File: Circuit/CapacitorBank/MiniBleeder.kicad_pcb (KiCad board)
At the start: 2 copper layers, 71.1 x 15.2 mm, 27 parts, among them J1 Signal 1/3, J2 Signal 2/4, J3 Power

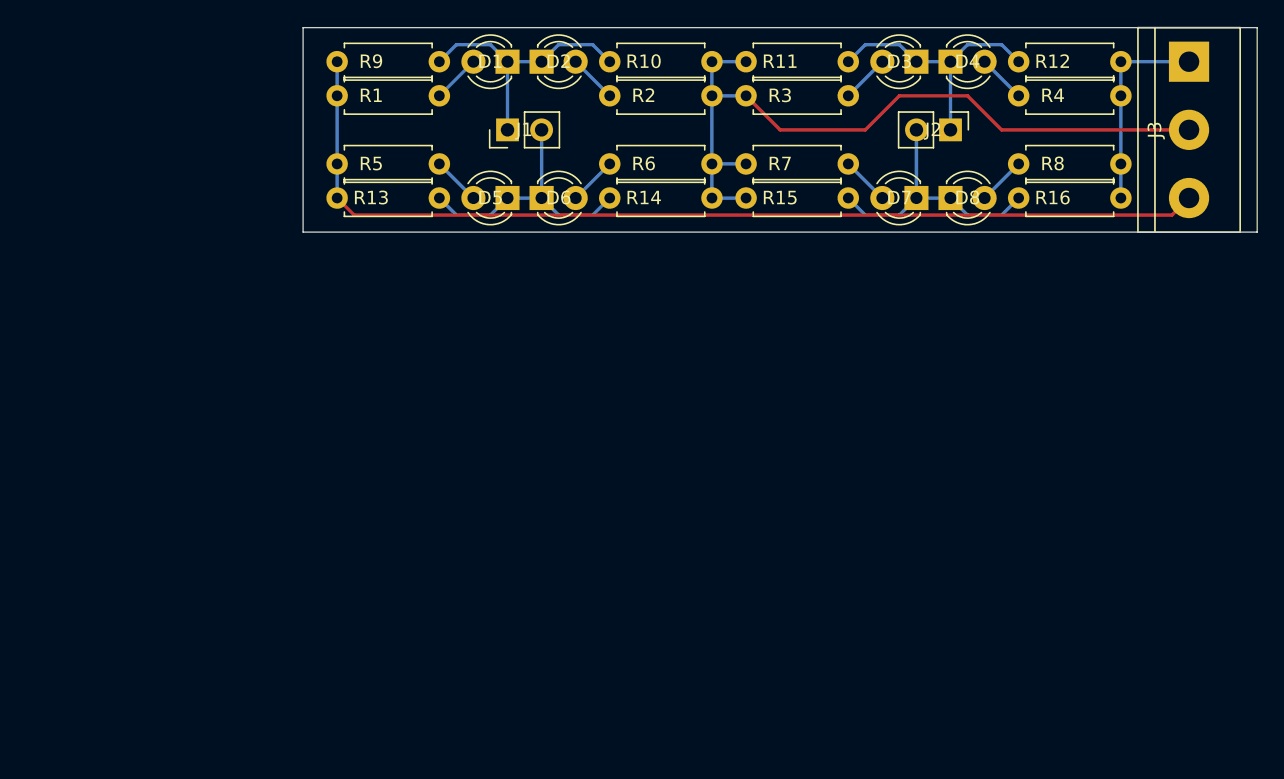
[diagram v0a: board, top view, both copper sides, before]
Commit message: [Circuit] Polarized capacitor bank and bleeder
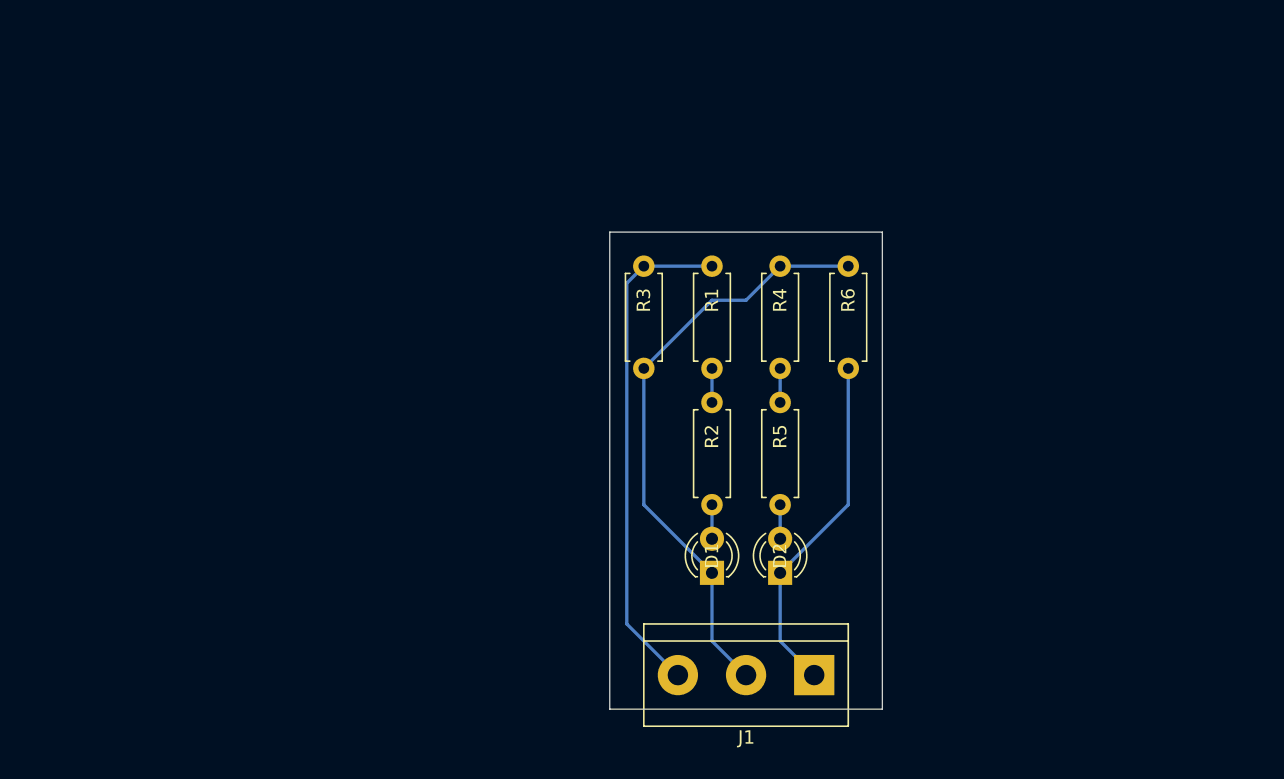
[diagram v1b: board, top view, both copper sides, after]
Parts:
- removed the D2 at (68.6, 53.3)
- removed D4, D5, D6, D7, D8: LED, LED_THT:LED_D3.0mm_FlatTop
- removed J2: Signal 2/4, Connector_PinHeader_2.54mm:PinHeader_1x02_P2.54mm_Vertical
- removed J3: Power, TerminalBlock:TerminalBlock_bornier-3_P5.08mm
- removed R10, R11, R12, R13, R14, R15, R16, R7, R8: 6.8K, Resistor_THT:R_Axial_DIN0207_L6.3mm_D2.5mm_P7.62mm_Horizontal
- removed the R3 at (83.8, 55.9)
- J1: value Signal 1/3 -> From Capacitor Bank; footprint Connector_PinHeader_2.54mm:PinHeader_1x02_P2.54mm_Vertical -> TerminalBlock:TerminalBlock_bornier-3_P5.08mm
- R1, R4: value 6.8K -> 10K
- R2, R5: value 6.8K -> 3.3K
- R3: renamed from R9; value 6.8K -> 20K
- R6: value 6.8K -> 20K
- moved J1 46.6 mm to (88.9, 99.1), turned to 180 degrees
- moved D1 41.0 mm to (81.3, 91.4), turned to 90 degrees
- moved D2 39.4 mm to (86.4, 91.4), turned to 90 degrees
- moved R5 37.5 mm to (86.4, 78.7), turned to 270 degrees
- moved R1 30.7 mm to (81.3, 68.6), turned to 270 degrees
- moved R3 27.5 mm to (76.2, 68.6), turned to 270 degrees
- moved R2 24.1 mm to (81.3, 78.7), turned to 270 degrees
- moved R4 21.8 mm to (86.4, 68.6), turned to 270 degrees
- moved R6 19.3 mm to (91.4, 68.6), turned to 270 degrees
- renumbered D3 to D2
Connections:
- D1 pad 1: Net-(D1-Pad1) -> /CapacitorCenter
- D2 pad 1: Net-(D3-Pad1) -> /CapacitorPower-
- D2 pad 2: Net-(D3-Pad2) -> Net-(D2-Pad2)
- J1 pad 1: Net-(D1-Pad1) -> /CapacitorPower-
- J1 pad 2: Net-(D5-Pad1) -> /CapacitorCenter
- R1 pad 1: +VDC -> /CapacitorPower+
- R1 pad 2: Net-(D1-Pad2) -> Net-(R1-Pad2)
- R2 pad 1: Net-(D2-Pad2) -> Net-(R1-Pad2)
- R2 pad 2: GND -> Net-(D1-Pad2)
- R3 pad 1: +VDC -> /CapacitorPower+
- R3 pad 2: Net-(D1-Pad1) -> /CapacitorCenter
- R4 pad 1: Net-(D4-Pad2) -> /CapacitorCenter
- R4 pad 2: -VDC -> Net-(R4-Pad2)
- R5 pad 1: +VDC -> Net-(R4-Pad2)
- R5 pad 2: Net-(D5-Pad2) -> Net-(D2-Pad2)
- R6 pad 1: Net-(D6-Pad2) -> /CapacitorCenter
- R6 pad 2: GND -> /CapacitorPower-
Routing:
- net +VDC: track 74.7 -> 0.00 mm
- net GND: track 56.5 -> 0.00 mm
- net /CapacitorCenter: track 0.00 -> 44.4 mm
- net /CapacitorPower+: track 0.00 -> 37.7 mm
- net /CapacitorPower-: track 0.00 -> 26.0 mm
- net Net-(D3-Pad1): track 19.9 -> 0.00 mm
- net Net-(D1-Pad1): track 19.9 -> 0.00 mm
- net Net-(D7-Pad1): track 19.9 -> 0.00 mm
- net Net-(D5-Pad1): track 19.9 -> 0.00 mm
- net -VDC: track 15.2 -> 0.00 mm
- net Net-(D8-Pad2): track 3.59 -> 0.00 mm
- net Net-(D7-Pad2): track 3.59 -> 0.00 mm
- net Net-(D4-Pad2): track 3.59 -> 0.00 mm
- net Net-(D3-Pad2): track 3.59 -> 0.00 mm
- net Net-(D5-Pad2): track 3.59 -> 0.00 mm
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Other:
- board size 71.1 x 15.2 mm -> 20.3 x 35.6 mm

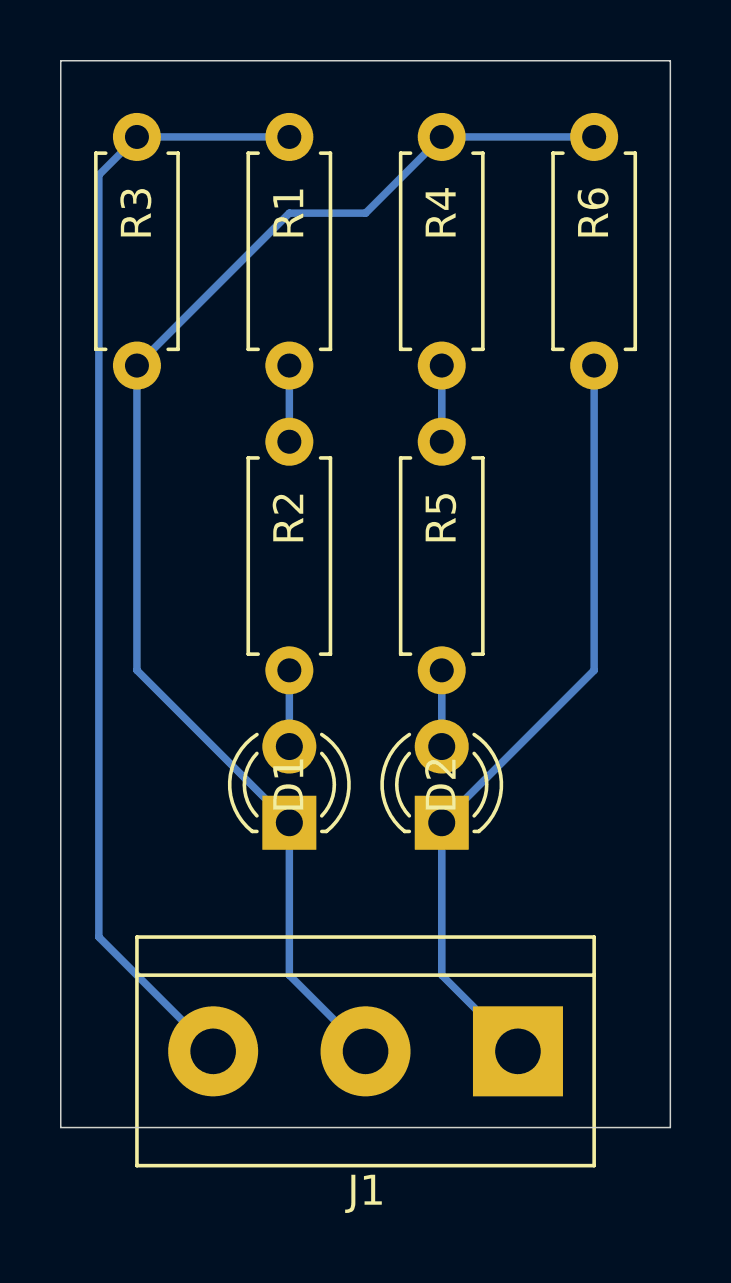
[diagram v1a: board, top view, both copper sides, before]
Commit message: [Circuit] Update the numbers in capacitor bank subsystem
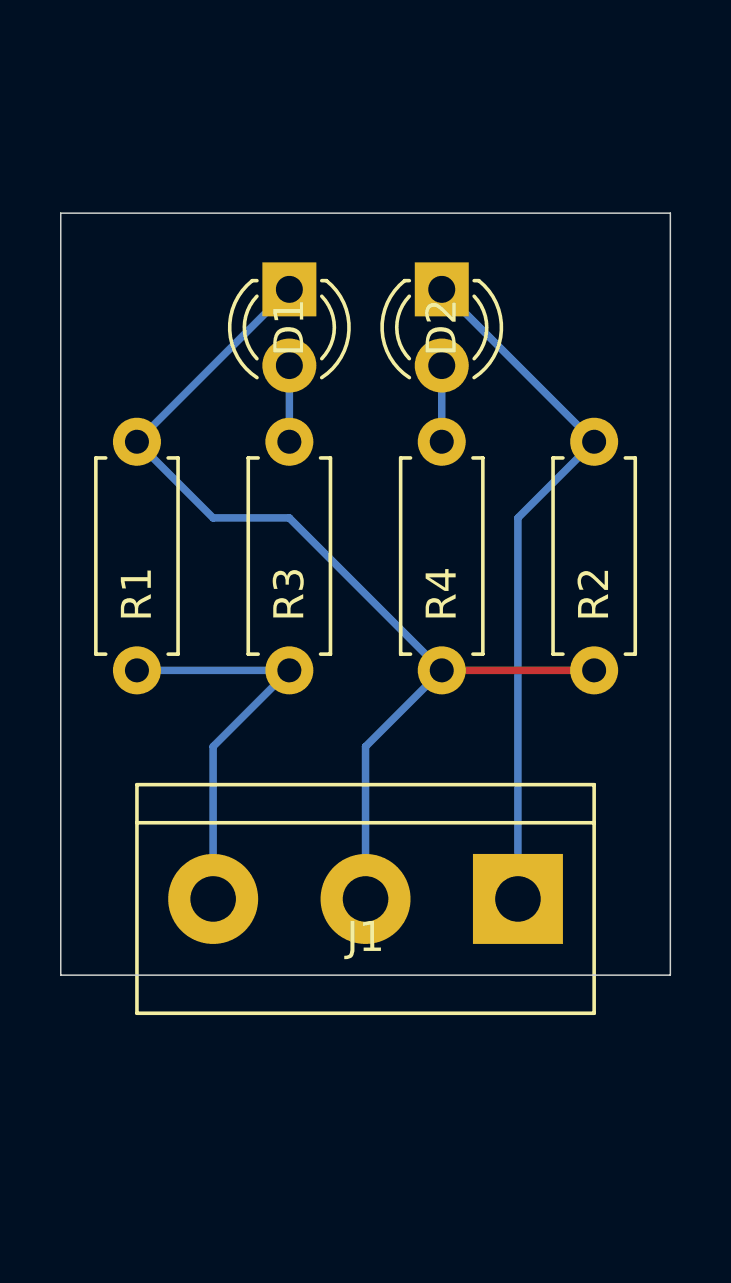
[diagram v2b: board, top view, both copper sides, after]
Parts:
- removed the R3 at (76.2, 68.6)
- removed the R4 at (86.4, 68.6)
- removed R6: 20K, Resistor_THT:R_Axial_DIN0207_L6.3mm_D2.5mm_P7.62mm_Horizontal
- added R2: 20K, Resistor_THT:R_Axial_DIN0207_L6.3mm_D2.5mm_P7.62mm_Horizontal, F.Cu at (91.4, 86.4)
- R1: value 10K -> 20K
- moved R1 18.5 mm to (76.2, 86.4), turned to 90 degrees
- moved D1 17.8 mm to (81.3, 73.7), turned to 270 degrees
- moved D2 17.8 mm to (86.4, 73.7), turned to 270 degrees
- moved R3 7.62 mm to (81.3, 86.4), turned to 90 degrees
- moved R4 7.62 mm to (86.4, 86.4), turned to 90 degrees
- moved J1 5.08 mm to (88.9, 94.0)
- renumbered R2 to R3, R5 to R4
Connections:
- R1 pad 2: Net-(R1-Pad2) -> /CapacitorCenter
- R3 pad 1: Net-(R1-Pad2) -> /CapacitorPower+
- R4 pad 1: Net-(R4-Pad2) -> /CapacitorCenter
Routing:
- net /CapacitorPower+: track 37.7 -> 13.8 mm
- net /CapacitorCenter: track 44.4 -> 34.3 mm
- net /CapacitorPower-: track 26.0 -> 23.5 mm
- net Net-(R4-Pad2): track 2.54 -> 0.00 mm
- net Net-(R1-Pad2): track 2.54 -> 0.00 mm
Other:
- board size 20.3 x 35.6 mm -> 20.3 x 25.4 mm

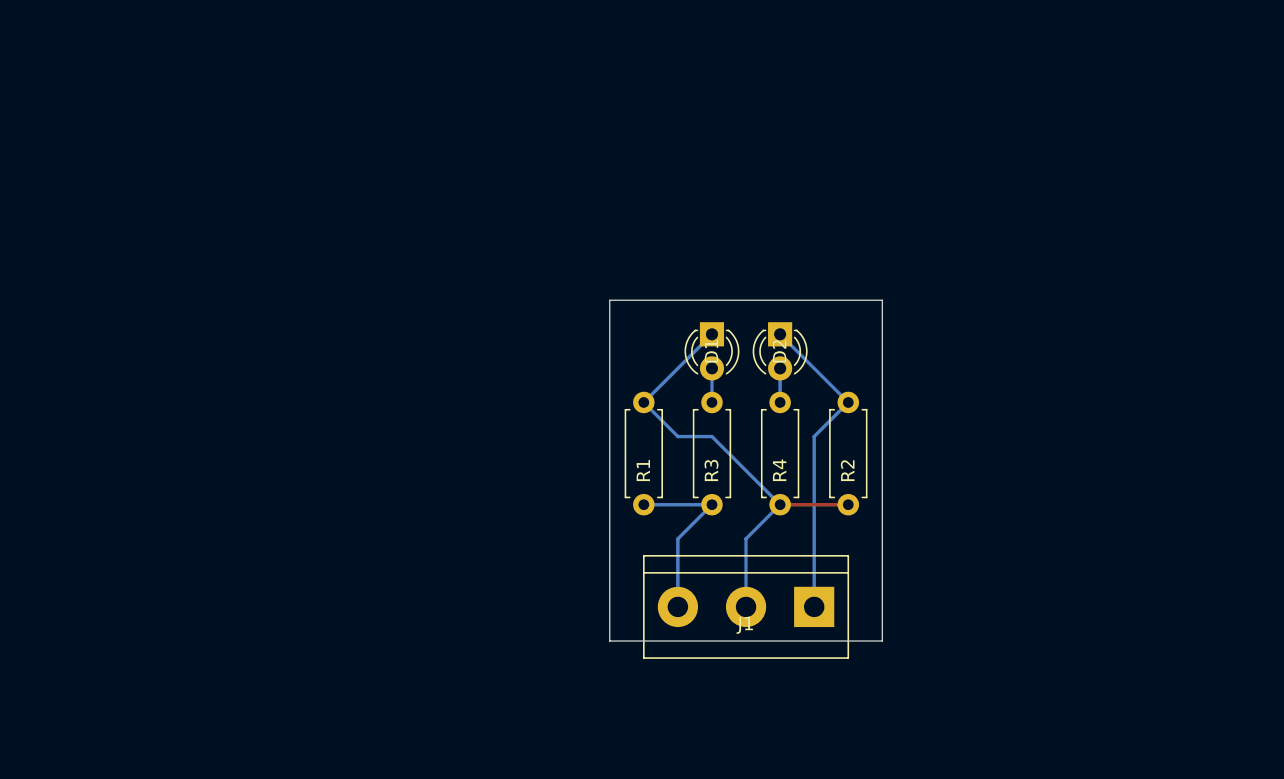
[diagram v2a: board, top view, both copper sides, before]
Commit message: [Circuit] Add isolated switches to bleeder circuits
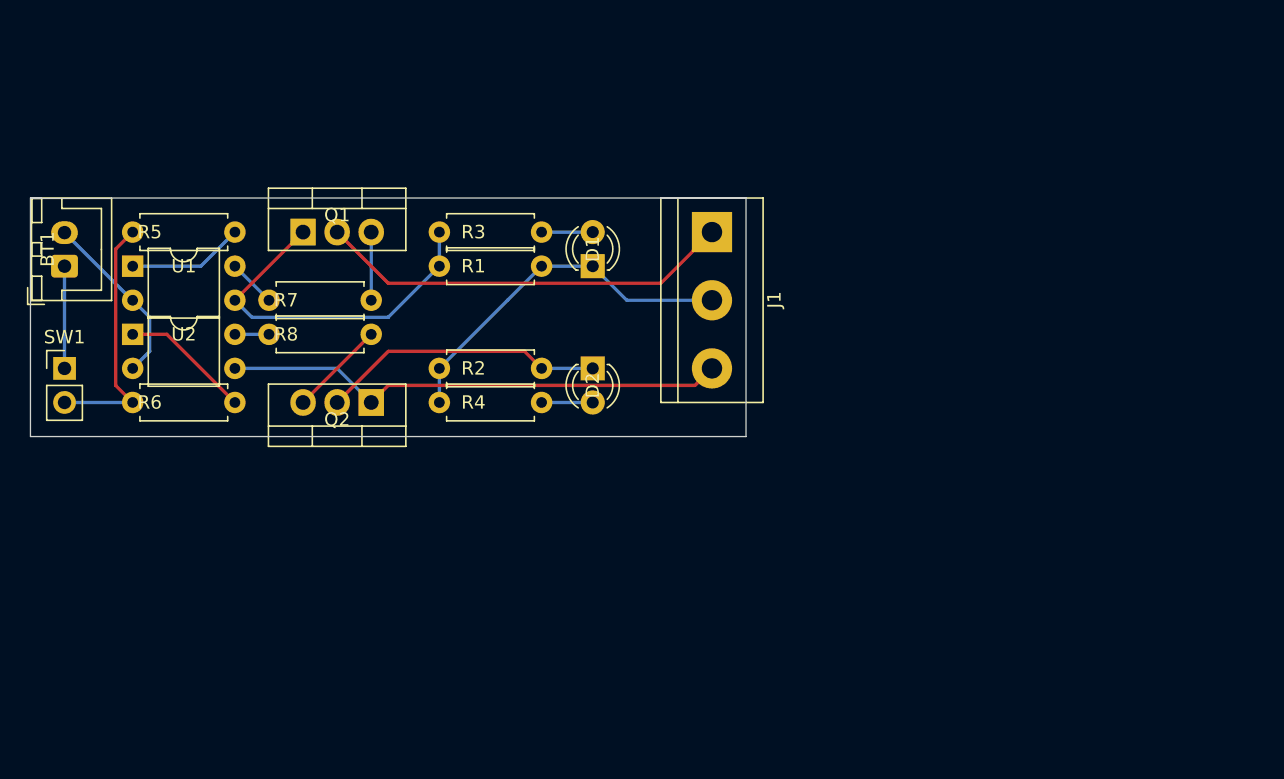
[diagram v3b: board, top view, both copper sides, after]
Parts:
- added BT1: 12V Battery, Connector_JST:JST_XH_B2B-XH-A_1x02_P2.50mm_Vertical, F.Cu at (33.0, 68.6)
- added Q1: BT138-800, Package_TO_SOT_THT:TO-220-3_Vertical, F.Cu at (50.8, 66.0)
- added Q2: BT138-800, Package_TO_SOT_THT:TO-220-3_Vertical, F.Cu at (55.9, 78.7)
- added R5: 1K, Resistor_THT:R_Axial_DIN0207_L6.3mm_D2.5mm_P7.62mm_Horizontal, F.Cu at (38.1, 66.0)
- added R6: 1K, Resistor_THT:R_Axial_DIN0207_L6.3mm_D2.5mm_P7.62mm_Horizontal, F.Cu at (38.1, 78.7)
- added R7: 1K, Resistor_THT:R_Axial_DIN0207_L6.3mm_D2.5mm_P7.62mm_Horizontal, F.Cu at (55.9, 71.1)
- added R8: 1K, Resistor_THT:R_Axial_DIN0207_L6.3mm_D2.5mm_P7.62mm_Horizontal, F.Cu at (55.9, 73.7)
- added SW1: SW_Push, Connector_PinHeader_2.54mm:PinHeader_1x02_P2.54mm_Vertical, F.Cu at (33.0, 76.2)
- added U1: PC817, Package_DIP:DIP-4_W7.62mm, F.Cu at (38.1, 68.6)
- added U2: PC817, Package_DIP:DIP-4_W7.62mm, F.Cu at (38.1, 73.7)
- moved R2 32.1 mm to (61.0, 76.2), turned to 0 degrees
- moved J1 29.0 mm to (81.3, 66.0), turned to 270 degrees
- moved R3 28.7 mm to (61.0, 66.0), turned to 0 degrees
- moved R4 26.5 mm to (61.0, 78.7), turned to 0 degrees
- moved R1 23.4 mm to (61.0, 68.6), turned to 0 degrees
- moved D2 14.2 mm to (72.4, 76.2)
- moved D1 10.2 mm to (72.4, 68.6), turned to 90 degrees
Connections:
- D2 pad 1: /CapacitorPower- -> Net-(D2-Pad1)
- J1 pad 1: /CapacitorPower- -> /CapacitorPower+
- J1 pad 3: /CapacitorPower+ -> /CapacitorPower-
- R1 pad 1: /CapacitorPower+ -> Net-(Q1-Pad1)
- R2 pad 2: /CapacitorPower- -> Net-(D2-Pad1)
- R3 pad 1: /CapacitorPower+ -> Net-(Q1-Pad1)
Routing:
- net Net-(Q1-Pad1): track 0.00 -> 27.1 mm
- net Net-(D2-Pad1): track 0.00 -> 21.2 mm
- net Net-(R5-Pad1): track 0.00 -> 18.8 mm
- net /CapacitorPower+: track 13.8 -> 31.1 mm
- net /CapacitorPower-: track 23.5 -> 37.7 mm
- net Net-(BT1-Pad2): track 0.00 -> 13.4 mm
- net Net-(R6-Pad2): track 0.00 -> 9.72 mm
- net Net-(R5-Pad2): track 0.00 -> 8.67 mm
- net Net-(BT1-Pad1): track 0.00 -> 7.62 mm
- net /CapacitorCenter: track 34.3 -> 27.1 mm
- net Net-(Q2-Pad3): track 0.00 -> 7.18 mm
- net Net-(Q1-Pad3): track 0.00 -> 5.08 mm
- net Net-(R7-Pad2): track 0.00 -> 3.59 mm
- net Net-(R8-Pad2): track 0.00 -> 2.54 mm
- net Net-(D2-Pad2): track 2.54 -> 3.81 mm
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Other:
- board size 20.3 x 25.4 mm -> 53.3 x 17.8 mm
